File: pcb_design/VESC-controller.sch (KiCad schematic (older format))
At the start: 30 parts, among them J1 GATE_DRIVER_CONN_U, J2 GATE_DRIVER_CONN_V, J3 GATE_DRIVER_CONN_W, J4 micro USB, J5 ACCEL, J6 REGEN, J7 12V, J8 V_BUS, P1 HALL/Encoder, P101 CANBUS, P2 Resolver, P3 PWR_COMM

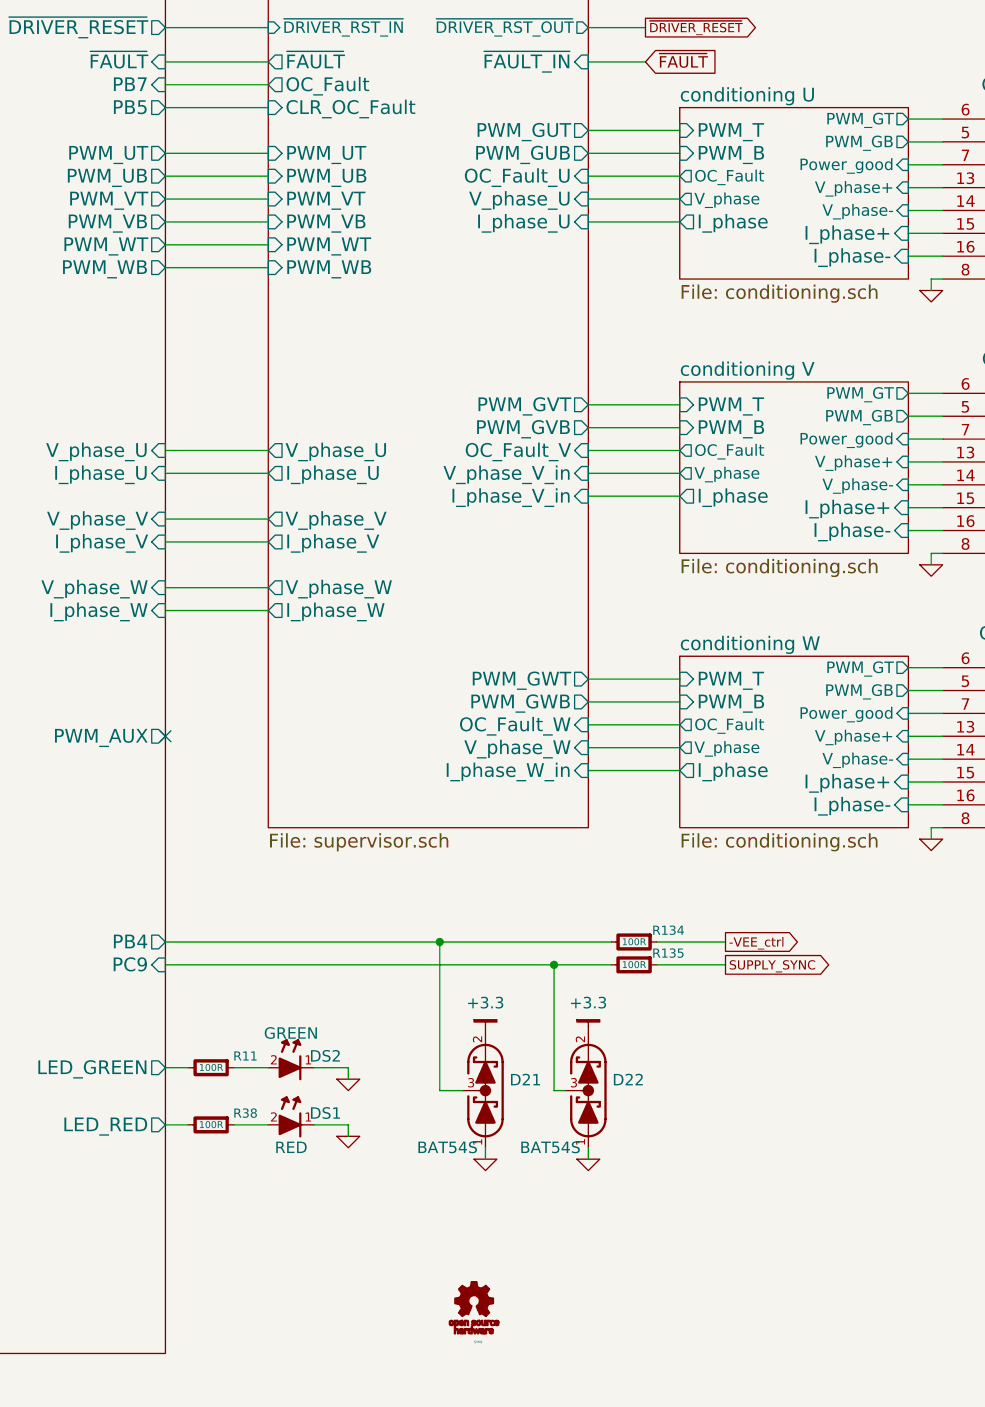
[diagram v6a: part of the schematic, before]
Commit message: Silkscreen logos, fixed swapped OCP inputs, added a button to enter bootloader,missing 3d model.
Signed-off-by: Marcos Chaparro <mchaparro@paltatech.com>
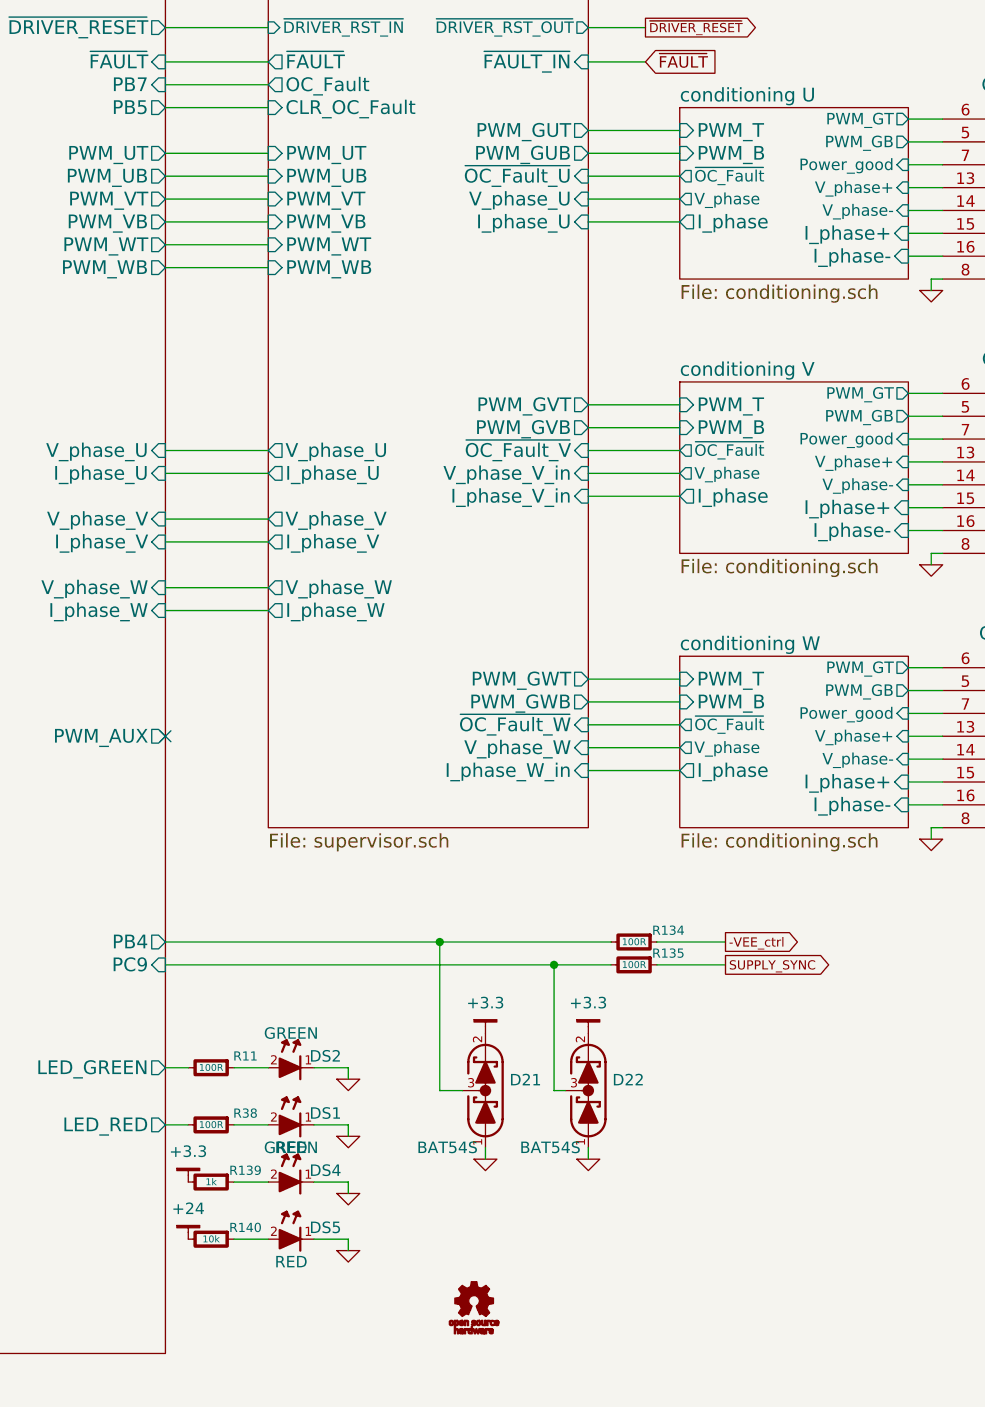
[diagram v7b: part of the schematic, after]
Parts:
- removed SYM1: OSHW-SCHEM-PCB10mm, symbol OSHW-SCHEM-PCB10mm
- added DS4: GREEN, smd-semi:LED-0603, symbol LED-0603
- added DS5: RED, smd-semi:LED-0603, symbol LED-0603
- added R139: 1k, IPC7351-Nominal:RESC1608X50, symbol R-0603
- added R140: 10k, IPC7351-Nominal:RESC1608X50, symbol R-0603
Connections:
- net +24: now also R140.2
- net +3.3: now also R139.2
- net GND: now also DS4.1 (K), DS5.1 (K)
- new net: DS5.2 (A), R140.1
- new net: DS4.2 (A), R139.1

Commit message: Updated component values according to simulations. 1.5khz for user inputs and  240khz lp pass filters for motor control
Signed-off-by: Marcos Chaparro <mchaparro@paltatech.com>
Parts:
- D21, D22: mfg# (none) -> TBAT54S,LM
- R103, R104: mfg# (none) -> RC0603FR-0722RL
- R11, R134, R135, R38: mfg# (none) -> RC0603FR-07100RL
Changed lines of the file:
@@
 F 2 "IPC7351-Nominal:RESC1608X50" V 2330 2750 30  0001 C CNN
 F 3 "" H 2400 2750 30  0000 C CNN
+F 4 "RC0603FR-0722RL" H 2400 2750 60  0001 C CNN "mfg#"
 	1    2400 2750
 	0    1    1    0
@@
 F 2 "IPC7351-Nominal:RESC1608X50" V 2330 2850 30  0001 C CNN
 F 3 "" H 2400 2850 30  0000 C CNN
+F 4 "RC0603FR-0722RL" H 2400 2850 60  0001 C CNN "mfg#"
 	1    2400 2850
 	0    1    1    0
@@
 F 2 "IPC7351-Nominal:RESC1608X50" V 5930 6400 30  0001 C CNN
 F 3 "" H 6000 6400 30  0000 C CNN
+F 4 "RC0603FR-07100RL" H 6000 6400 60  0001 C CNN "mfg#"
 	1    6000 6400
 	0    1    1    0
@@
 F 2 "IPC7351-Nominal:RESC1608X50" V 5930 6150 30  0001 C CNN
 F 3 "" H 6000 6150 30  0000 C CNN
+F 4 "RC0603FR-07100RL" H 6000 6150 60  0001 C CNN "mfg#"
 	1    6000 6150
 	0    1    1    0
@@
 F 2 "smd-semi:SOT-23" H 7650 6100 60  0001 C CNN
 F 3 "" V 7600 6250 60  0000 C CNN
-F 4 "SCHOTTKY BAT54S" H 7650 6000 60  0001 C CNN "BOM"
+F 4 "TBAT54S,LM" H 7650 6250 60  0001 C CNN "mfg#"
+F 5 "SCHOTTKY BAT54S" H 7650 6000 60  0001 C CNN "BOM"
 	1    7650 6250
 	0    -1   -1   0
@@
 F 2 "smd-semi:SOT-23" H 7200 6100 60  0001 C CNN
 F 3 "" V 7150 6250 60  0000 C CNN
-F 4 "SCHOTTKY BAT54S" H 7200 6000 60  0001 C CNN "BOM"
+F 4 "TBAT54S,LM" H 7200 6250 60  0001 C CNN "mfg#"
+F 5 "SCHOTTKY BAT54S" H 7200 6000 60  0001 C CNN "BOM"
 	1    7200 6250
 	0    -1   -1   0
@@
 F 2 "IPC7351-Nominal:RESC1608X50" V 7780 5700 30  0001 C CNN
 F 3 "" H 7850 5700 30  0000 C CNN
+F 4 "RC0603FR-07100RL" H 7850 5700 60  0001 C CNN "mfg#"
 	1    7850 5700
 	0    1    1    0
@@
 F 2 "IPC7351-Nominal:RESC1608X50" V 7780 5600 30  0001 C CNN
 F 3 "" H 7850 5600 30  0000 C CNN
+F 4 "RC0603FR-07100RL" H 7850 5600 60  0001 C CNN "mfg#"
 	1    7850 5600
 	0    1    1    0
